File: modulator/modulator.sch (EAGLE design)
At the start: 43 parts, among them IC1 LM741P, T2 BF173

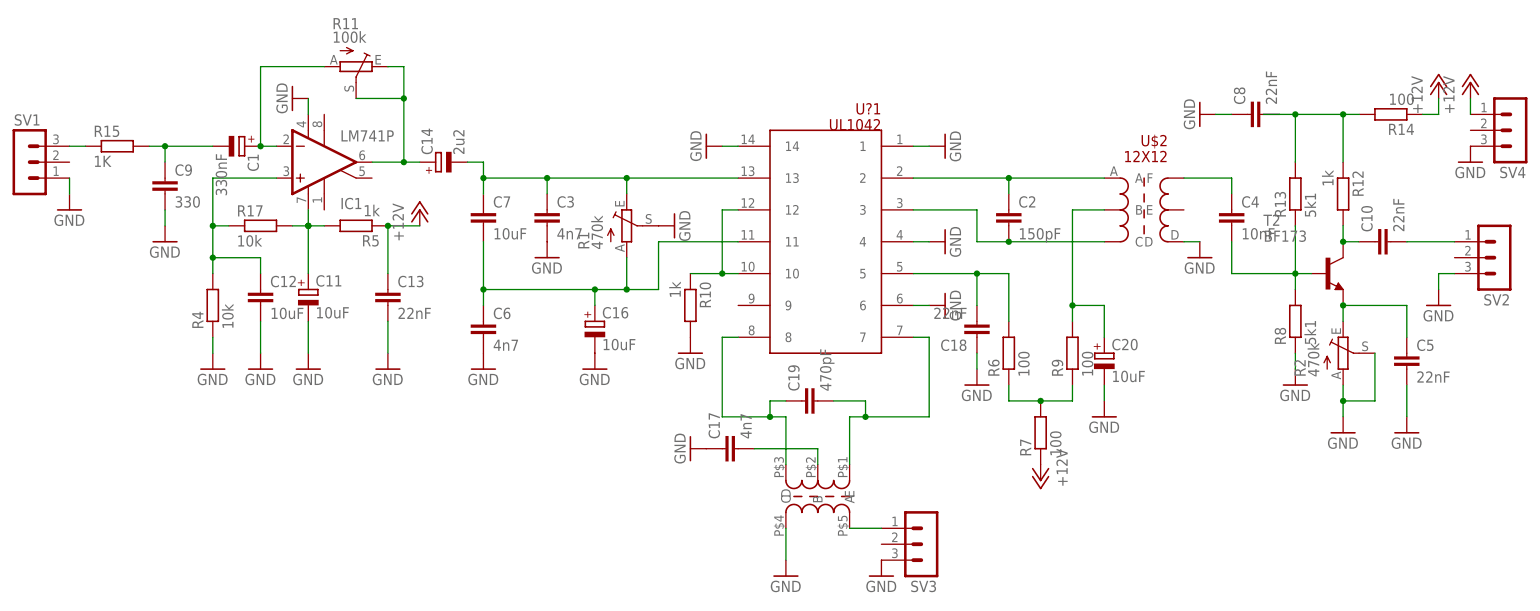
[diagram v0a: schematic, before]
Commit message: rearrange the elements on the PCB.
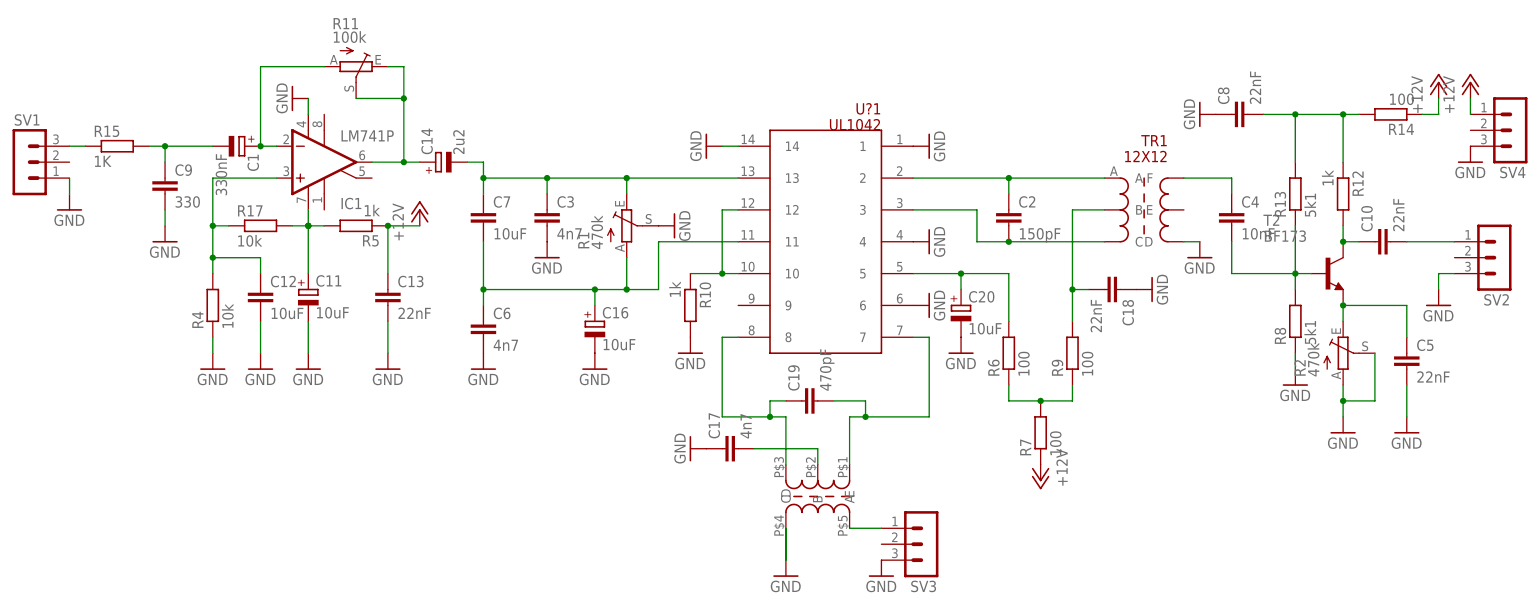
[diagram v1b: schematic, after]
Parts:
- renumbered U$2 to TR1, U$3 to TR2
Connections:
- net N$11: now also C20.+; no longer C18.2
- net N$21: now also C18.2; no longer C20.+
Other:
- moved on the sheet: C18, C20, C8
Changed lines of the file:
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@@
 <part name="GND12" library="supply1" deviceset="GND" device=""/>
 <part name="GND13" library="supply1" deviceset="GND" device=""/>
-<part name="U$2" library="sp5ww" deviceset="12X12" device=""/>
+<part name="TR1" library="sp5ww" deviceset="12X12" device=""/>
 <part name="GND14" library="supply1" deviceset="GND" device=""/>
 <part name="GND15" library="supply1" deviceset="GND" device=""/>
-<part name="U$3" library="sp5ww" deviceset="TR5X5" device=""/>
+<part name="TR2" library="sp5ww" deviceset="TR5X5" device=""/>
 <part name="GND16" library="supply1" deviceset="GND" device=""/>
 <part name="GND17" library="supply1" deviceset="GND" device=""/>
@@
 <instance part="U?1" gate="G$1" x="91.44" y="25.4" rot="MR0"/>
 <instance part="GND7" gate="1" x="81.28" y="58.42" rot="R270"/>
-<instance part="GND8" gate="1" x="119.38" y="58.42" rot="R90"/>
+<instance part="GND8" gate="1" x="116.84" y="58.42" rot="R90"/>
 <instance part="GND9" gate="1" x="78.74" y="25.4"/>
-<instance part="GND10" gate="1" x="119.38" y="43.18" rot="R90"/>
-<instance part="GND11" gate="1" x="119.38" y="33.02" rot="R90"/>
+<instance part="GND10" gate="1" x="116.84" y="43.18" rot="R90"/>
+<instance part="GND11" gate="1" x="116.84" y="33.02" rot="R90"/>
 <instance part="T2" gate="G$1" x="180.34" y="38.1"/>
 <instance part="GND12" gate="1" x="76.2" y="45.72" rot="R90"/>
 <instance part="GND13" gate="1" x="45.72" y="22.86"/>
-<instance part="U$2" gate="G$1" x="142.24" y="48.26" rot="MR0"/>
-<instance part="GND14" gate="1" x="124.46" y="20.32"/>
+<instance part="TR1" gate="G$1" x="142.24" y="48.26" rot="MR0"/>
+<instance part="GND14" gate="1" x="152.4" y="35.56" rot="R90"/>
 <instance part="GND15" gate="1" x="160.02" y="40.64"/>
-<instance part="U$3" gate="G$1" x="86.36" y="-30.48" rot="R270"/>
+<instance part="TR2" gate="G$1" x="86.36" y="-30.48" rot="R270"/>
 <instance part="GND16" gate="1" x="78.74" y="10.16" rot="R270"/>
 <instance part="GND17" gate="1" x="55.88" y="40.64"/>
@@
 <instance part="GND21" gate="1" x="160.02" y="63.5" rot="R270"/>
 <instance part="GND22" gate="1" x="63.5" y="22.86"/>
-<instance part="GND23" gate="1" x="144.78" y="15.24"/>
+<instance part="GND23" gate="1" x="121.92" y="25.4"/>
 <instance part="GND24" gate="1" x="193.04" y="12.7"/>
 <instance part="12V_N2" gate="1" x="198.12" y="68.58"/>
@@
 <instance part="C4" gate="G$1" x="165.1" y="48.26"/>
 <instance part="C17" gate="G$1" x="83.82" y="10.16" rot="R90"/>
-<instance part="C8" gate="G$1" x="167.64" y="63.5" rot="R90"/>
-<instance part="C18" gate="G$1" x="124.46" y="27.94" rot="R180"/>
+<instance part="C8" gate="G$1" x="165.1" y="63.5" rot="R90"/>
+<instance part="C18" gate="G$1" x="147.32" y="35.56" rot="R270"/>
 <instance part="12V_N4" gate="1" x="35.56" y="48.26"/>
 <instance part="12V_N1" gate="1" x="134.62" y="5.08" rot="R180"/>
 <instance part="C19" gate="G$1" x="96.52" y="17.78" rot="R90"/>
-<instance part="C20" gate="G$1" x="144.78" y="25.4"/>
+<instance part="C20" gate="G$1" x="121.92" y="33.02"/>
 </instances>
 <busses>
@@
 <pinref part="U?1" gate="G$1" pin="1"/>
 <pinref part="GND8" gate="1" pin="GND"/>
-<wire x1="114.3" y1="58.42" x2="116.84" y2="58.42" width="0.1524" layer="91"/>
 </segment>
 <segment>
 <pinref part="U?1" gate="G$1" pin="4"/>
 <pinref part="GND10" gate="1" pin="GND"/>
-<wire x1="114.3" y1="43.18" x2="116.84" y2="43.18" width="0.1524" layer="91"/>
 </segment>
 <segment>
 <pinref part="U?1" gate="G$1" pin="6"/>
 <pinref part="GND11" gate="1" pin="GND"/>
-<wire x1="114.3" y1="33.02" x2="116.84" y2="33.02" width="0.1524" layer="91"/>
 </segment>
 <segment>
@@
 <segment>
 <pinref part="GND14" gate="1" pin="GND"/>
-<wire x1="124.46" y1="25.4" x2="124.46" y2="22.86" width="0.1524" layer="91"/>
 <pinref part="C18" gate="G$1" pin="1"/>
 </segment>
@@
 <segment>
 <pinref part="GND21" gate="1" pin="GND"/>
-<wire x1="165.1" y1="63.5" x2="162.56" y2="63.5" width="0.1524" layer="91"/>
 <pinref part="C8" gate="G$1" pin="1"/>
 </segment>
 <segment>
-<pinref part="U$3" gate="G$1" pin="D"/>
+<pinref part="TR2" gate="G$1" pin="D"/>
 <pinref part="GND19" gate="1" pin="GND"/>
 <wire x1="93.98" y1="-2.54" x2="93.98" y2="-7.62" width="0.1524" layer="91"/>
+<wire x1="93.98" y1="-2.54" x2="93.98" y2="-7.62" width="0.1524" layer="91"/>
 </segment>
 <segment>
@@
 <segment>
 <pinref part="GND23" gate="1" pin="GND"/>
-<wire x1="144.78" y1="20.32" x2="144.78" y2="17.78" width="0.1524" layer="91"/>
 <pinref part="C20" gate="G$1" pin="-"/>
 </segment>
@@
 </segment>
 <segment>
-<pinref part="U$2" gate="G$1" pin="D"/>
+<pinref part="TR1" gate="G$1" pin="D"/>
 <pinref part="GND15" gate="1" pin="GND"/>
 <wire x1="157.48" y1="43.18" x2="160.02" y2="43.18" width="0.1524" layer="91"/>
@@
 <segment>
 <pinref part="U?1" gate="G$1" pin="2"/>
-<pinref part="U$2" gate="G$1" pin="A"/>
+<pinref part="TR1" gate="G$1" pin="A"/>
 <wire x1="114.3" y1="53.34" x2="129.54" y2="53.34" width="0.1524" layer="91"/>
 <wire x1="129.54" y1="53.34" x2="144.78" y2="53.34" width="0.1524" layer="91"/>
@@
 <wire x1="114.3" y1="48.26" x2="124.46" y2="48.26" width="0.1524" layer="91"/>
 <wire x1="124.46" y1="48.26" x2="124.46" y2="43.18" width="0.1524" layer="91"/>
-<pinref part="U$2" gate="G$1" pin="C"/>
+<pinref part="TR1" gate="G$1" pin="C"/>
 <wire x1="124.46" y1="43.18" x2="129.54" y2="43.18" width="0.1524" layer="91"/>
 <pinref part="C2" gate="G$1" pin="2"/>
@@
 <segment>
 <pinref part="U?1" gate="G$1" pin="5"/>
-<wire x1="124.46" y1="38.1" x2="114.3" y2="38.1" width="0.1524" layer="91"/>
-<wire x1="124.46" y1="33.02" x2="124.46" y2="38.1" width="0.1524" layer="91"/>
-<wire x1="124.46" y1="38.1" x2="129.54" y2="38.1" width="0.1524" layer="91"/>
+<wire x1="129.54" y1="38.1" x2="121.92" y2="38.1" width="0.1524" layer="91"/>
+<wire x1="121.92" y1="38.1" x2="114.3" y2="38.1" width="0.1524" layer="91"/>
 <wire x1="129.54" y1="38.1" x2="129.54" y2="30.48" width="0.1524" layer="91"/>
-<junction x="124.46" y="38.1"/>
 <pinref part="R6" gate="G$1" pin="2"/>
-<pinref part="C18" gate="G$1" pin="2"/>
+<pinref part="C20" gate="G$1" pin="+"/>
+<wire x1="121.92" y1="35.56" x2="121.92" y2="38.1" width="0.1524" layer="91"/>
+<junction x="121.92" y="38.1"/>
 </segment>
 </net>
@@
 <wire x1="83.82" y1="27.94" x2="83.82" y2="15.24" width="0.1524" layer="91"/>
 <wire x1="83.82" y1="15.24" x2="91.44" y2="15.24" width="0.1524" layer="91"/>
-<pinref part="U$3" gate="G$1" pin="C"/>
+<pinref part="TR2" gate="G$1" pin="C"/>
 <wire x1="91.44" y1="15.24" x2="93.98" y2="15.24" width="0.1524" layer="91"/>
 <wire x1="93.98" y1="15.24" x2="93.98" y2="7.62" width="0.1524" layer="91"/>
@@
 <wire x1="116.84" y1="27.94" x2="116.84" y2="15.24" width="0.1524" layer="91"/>
 <wire x1="116.84" y1="15.24" x2="106.68" y2="15.24" width="0.1524" layer="91"/>
-<pinref part="U$3" gate="G$1" pin="A"/>
+<pinref part="TR2" gate="G$1" pin="A"/>
 <wire x1="106.68" y1="15.24" x2="104.14" y2="15.24" width="0.1524" layer="91"/>
 <wire x1="104.14" y1="15.24" x2="104.14" y2="7.62" width="0.1524" layer="91"/>
@@
 <segment>
 <wire x1="175.26" y1="55.88" x2="175.26" y2="63.5" width="0.1524" layer="91"/>
-<wire x1="175.26" y1="63.5" x2="172.72" y2="63.5" width="0.1524" layer="91"/>
 <wire x1="182.88" y1="55.88" x2="182.88" y2="63.5" width="0.1524" layer="91"/>
 <wire x1="182.88" y1="63.5" x2="175.26" y2="63.5" width="0.1524" layer="91"/>
 <wire x1="185.42" y1="63.5" x2="182.88" y2="63.5" width="0.1524" layer="91"/>
-<junction x="175.26" y="63.5"/>
 <junction x="182.88" y="63.5"/>
 <pinref part="R12" gate="G$1" pin="1"/>
@@
 <pinref part="R14" gate="G$1" pin="2"/>
 <pinref part="C8" gate="G$1" pin="2"/>
-<wire x1="172.72" y1="63.5" x2="170.18" y2="63.5" width="0.1524" layer="91"/>
+<wire x1="170.18" y1="63.5" x2="175.26" y2="63.5" width="0.1524" layer="91"/>
+<junction x="175.26" y="63.5"/>
 </segment>
 </net>
@@
 <net name="N$21" class="0">
 <segment>
-<wire x1="139.7" y1="33.02" x2="139.7" y2="30.48" width="0.1524" layer="91"/>
-<wire x1="144.78" y1="27.94" x2="144.78" y2="33.02" width="0.1524" layer="91"/>
-<wire x1="144.78" y1="33.02" x2="139.7" y2="33.02" width="0.1524" layer="91"/>
-<junction x="139.7" y="33.02"/>
-<wire x1="139.7" y1="33.02" x2="139.7" y2="48.26" width="0.1524" layer="91"/>
-<pinref part="U$2" gate="G$1" pin="B"/>
+<wire x1="139.7" y1="30.48" x2="139.7" y2="35.56" width="0.1524" layer="91"/>
+<pinref part="TR1" gate="G$1" pin="B"/>
+<wire x1="139.7" y1="35.56" x2="139.7" y2="48.26" width="0.1524" layer="91"/>
 <wire x1="139.7" y1="48.26" x2="144.78" y2="48.26" width="0.1524" layer="91"/>
 <pinref part="R9" gate="G$1" pin="2"/>
-<pinref part="C20" gate="G$1" pin="+"/>
+<pinref part="C18" gate="G$1" pin="2"/>
+<wire x1="142.24" y1="35.56" x2="139.7" y2="35.56" width="0.1524" layer="91"/>
+<junction x="139.7" y="35.56"/>
 </segment>
 </net>
@@
 <net name="N$22" class="0">
 <segment>
-<pinref part="U$3" gate="G$1" pin="E"/>
+<pinref part="TR2" gate="G$1" pin="E"/>
 <wire x1="104.14" y1="-2.54" x2="109.22" y2="-2.54" width="0.1524" layer="91"/>
 <pinref part="SV3" gate="G$1" pin="1"/>
@@
 <net name="N$25" class="0">
 <segment>
-<pinref part="U$2" gate="G$1" pin="F"/>
+<pinref part="TR1" gate="G$1" pin="F"/>
 <wire x1="165.1" y1="53.34" x2="157.48" y2="53.34" width="0.1524" layer="91"/>
 <wire x1="165.1" y1="50.8" x2="165.1" y2="53.34" width="0.1524" layer="91"/>
@@
 <net name="N$12" class="0">
 <segment>
-<pinref part="U$3" gate="G$1" pin="B"/>
+<pinref part="TR2" gate="G$1" pin="B"/>
 <wire x1="99.06" y1="7.62" x2="99.06" y2="10.16" width="0.1524" layer="91"/>
 <pinref part="C17" gate="G$1" pin="2"/>
